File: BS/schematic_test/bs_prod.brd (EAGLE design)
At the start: 92 x 50 mm, 20 parts, among them U1 ATMEGA328P_PDIP, U2 RFM69HW, Y1 16MHz

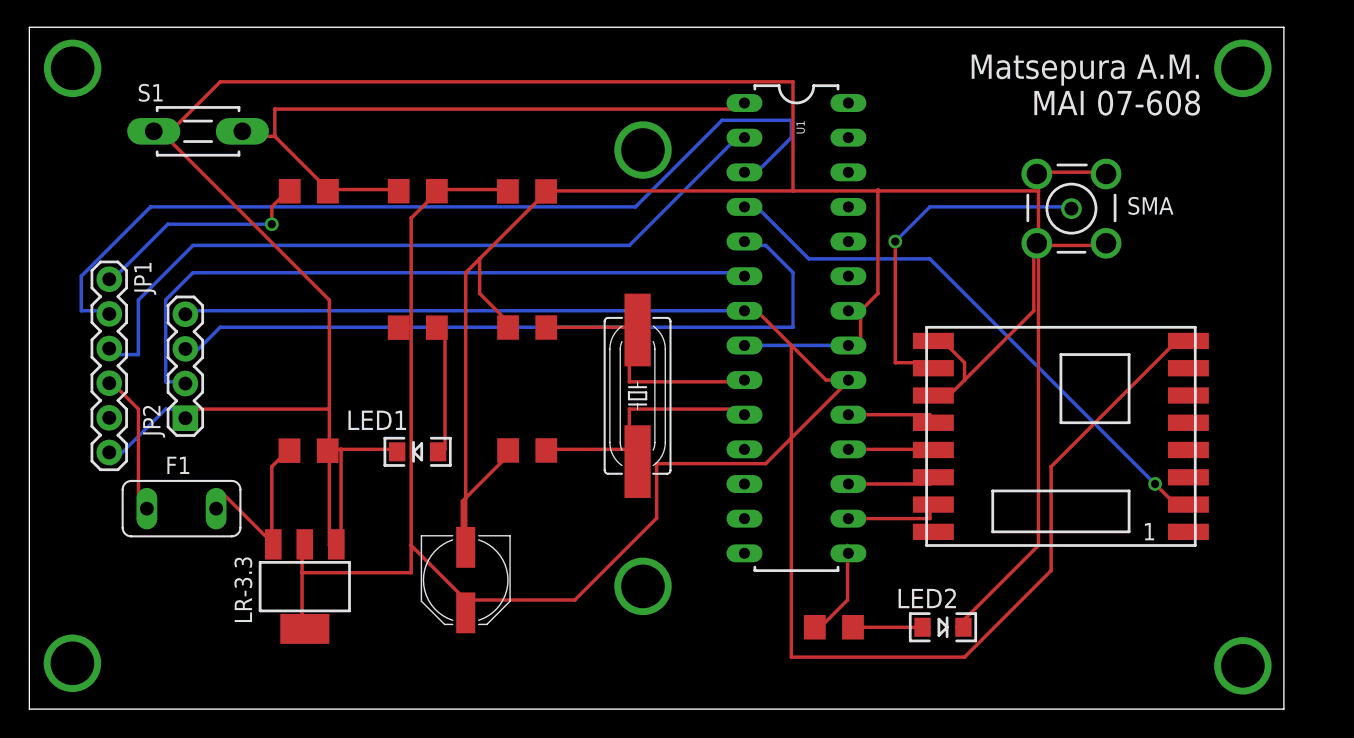
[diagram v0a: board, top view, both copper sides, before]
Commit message: BS schematic prod test add
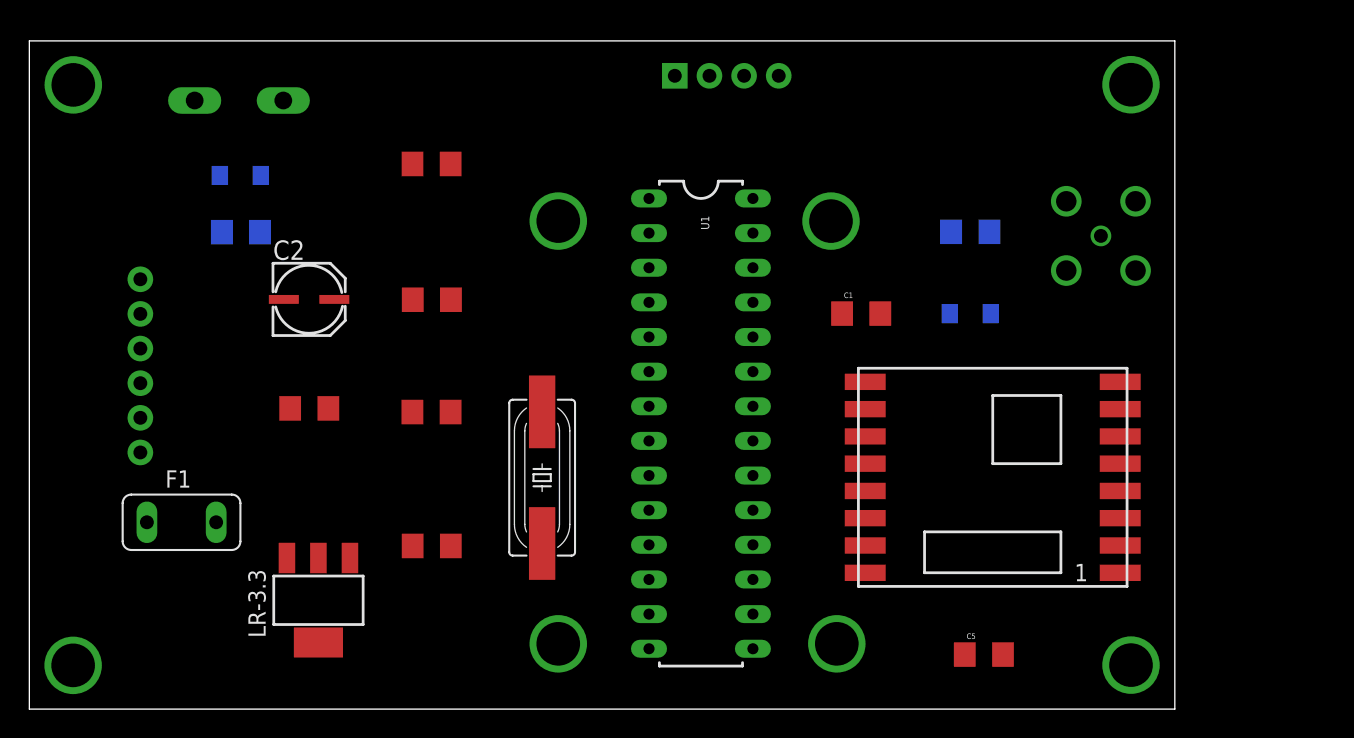
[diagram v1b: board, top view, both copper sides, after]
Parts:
- added C2: (no value), SparkFun-Capacitors:PANASONIC_C
- C1: value 10uF -> 0.1uF; device SparkFun-Capacitors:PANASONIC_D -> SparkFun-Capacitors:1206
- F1: value 500мА -> 500mA
- moved C5 47.7 mm to (70.0, 4.00)
- moved JP2 43.8 mm to (47.3, 46.4), flipped to the bottom, turned to 180 degrees
- moved C1 35.0 mm to (61.0, 29.0), turned to 0 degrees
- moved R3 30.7 mm to (69.0, 35.0), flipped to the bottom, turned to 180 degrees
- moved LED1 24.1 mm to (15.5, 39.1), flipped to the bottom, turned to 0 degrees
- moved LED2 23.1 mm to (69.0, 29.0), flipped to the bottom, turned to 180 degrees
- moved R2 14.7 mm to (15.5, 35.0), flipped to the bottom
- moved C4 9.90 mm to (29.5, 12.0)
- moved U1 9.90 mm to (49.3, 20.9)
- moved C3 9.36 mm to (29.5, 21.8)
- moved C6 9.22 mm to (29.5, 40.0)
- moved Y1 9.22 mm to (37.6, 17.0)
- moved R1 8.03 mm to (29.5, 30.0), turned to 0 degrees
- moved U2 5.83 mm to (70.6, 17.0)
- moved S1 3.76 mm to (15.4, 44.6), flipped to the bottom, turned to 0 degrees
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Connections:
- new net N$16: C1.1, U1.21
- net 3.3V: now also C2.+; no longer C1.+
- net GND: now also C1.2, C2.-; no longer C1.-, U1.21
- net GPS_RX: now also U1.5; no longer U1.6
- net GPS_TX: now also U1.6; no longer U1.5
- net N$12: now also U1.23; no longer U1.15
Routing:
- net GND: track 294.6 -> 0.00 mm
- net 3.3V: track 212.0 -> 0.00 mm
- net D1_TX: track 67.2 -> 0.00 mm
- net D0_RX: track 55.9 -> 0.00 mm
- net GPS_TX: track 54.9 -> 0.00 mm
- net GPS_RX: track 51.9 -> 0.00 mm
- net RST: track 50.8 -> 0.00 mm
- net D2: track 41.5 -> 0.00 mm, vias 1 -> 0
- net N$8: track 25.9 -> 0.00 mm, vias 1 -> 0
- net N$7: track 20.0 -> 0.00 mm
- net N$6: track 19.1 -> 0.00 mm
- net N$11: track 16.7 -> 0.00 mm, vias 1 -> 0
- net 5V: track 14.7 -> 0.00 mm
- net N$9: track 11.9 -> 0.00 mm
- net N$5: track 10.0 -> 0.00 mm
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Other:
- board size 92 x 50 mm -> 84 x 49 mm
- board text removed: "Matsepura A.M. MAI 07-608"

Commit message: BS schematic prod
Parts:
- removed LED1: (no value), SparkFun-LED:LED-1206
- removed S1: DTS-3, switch-tact:DTS-3
- added C8, C9: 0.1uF, SparkFun-Capacitors:1206
- added JP3: (no value), SparkFun-Connectors:1X06
- added JP4: (no value), SparkFun-Connectors:1X05
- added PWR: (no value), SparkFun-LED:LED-1206
- added RESET: DTSM-3, switch-tact:DTSM-3
- added U$1: UBLOX, myGps:UBLOX
- C2: value (none) -> 10uF
- moved R2 29.8 mm to (8.51, 5.97)
- moved C5 28.1 mm to (81.0, 29.8), turned to 180 degrees
- moved C2 13.8 mm to (32.9, 24.3)
- moved JP1 13.7 mm to (3.86, 18.5), turned to 90 degrees
- moved C7 13.4 mm to (32.5, 16.0), turned to 0 degrees
- moved F1 12.7 mm to (20.2, 4.70)
- moved LED2 12.2 mm to (81.0, 31.0)
- moved R3 12.0 mm to (81.0, 36.0)
- moved LR-3.3 11.0 mm to (32.2, 6.98)
- moved C1 11.0 mm to (72.0, 30.0), turned to 270 degrees
- moved U1 11.0 mm to (60.3, 21.9)
- moved C3 11.0 mm to (40.5, 21.8)
- moved C6 11.0 mm to (40.5, 40.0)
- moved C4 11.0 mm to (40.5, 12.0)
- moved SMA 11.0 mm to (89.6, 34.7)
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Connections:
- new net A0: JP3.4, U1.28
- new net A1: JP3.3, U1.27
- new net A2: JP3.2, U1.26
- new net A3: JP3.1, U1.25
- new net D5: JP4.1, U1.11
- new net D6: JP4.2, U1.12
- new net D7: JP4.3, U1.13
- net 3.3V: now also C8.1, C9.1, JP3.5, JP4.4
- net GND: now also C8.2, C9.2, JP3.6, JP4.5, PWR.C, RESET.2; no longer LED1.C, S1.2
- net N$5: now also PWR.A; no longer LED1.A
- net RST: now also RESET.1; no longer S1.1
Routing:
- net GND: track 0.00 -> 335.6 mm, vias 0 -> 2
- net 3.3V: track 0.00 -> 233.8 mm, vias 0 -> 5
- net N$11: track 0.00 -> 59.2 mm, vias 0 -> 1
- net D0_RX: track 0.00 -> 57.7 mm
- net D1_TX: track 0.00 -> 57.7 mm
- net D2: track 0.00 -> 46.0 mm, vias 0 -> 1
- net RST: track 0.00 -> 44.1 mm, vias 0 -> 1
- net D5: track 0.00 -> 35.1 mm
- net D6: track 0.00 -> 33.1 mm
- net A3: track 0.00 -> 31.5 mm
- net D7: track 0.00 -> 29.2 mm
- net A2: track 0.00 -> 27.7 mm
- net N$9: track 0.00 -> 27.1 mm
- net N$8: track 0.00 -> 26.4 mm, vias 0 -> 1
- net A1: track 0.00 -> 23.2 mm
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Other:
- board size 84 x 49 mm -> 95 x 49 mm
- board text added: "+5V"
- board text added: "3V3"
- board text added: "A2"
- board text added: "A3"
- board text added: "CTS"
- board text added: "D5"
- board text added: "D6"
- board text added: "D7"
- board text added: "DTR"
- board text added: "GND"
- board text added: "Matsepura A.M. MAI 07-608"
- board text added: "RX"
- board text added: "SCL"
- board text added: "SDA"
- board text added: "TX"
- board text added: "TX\"

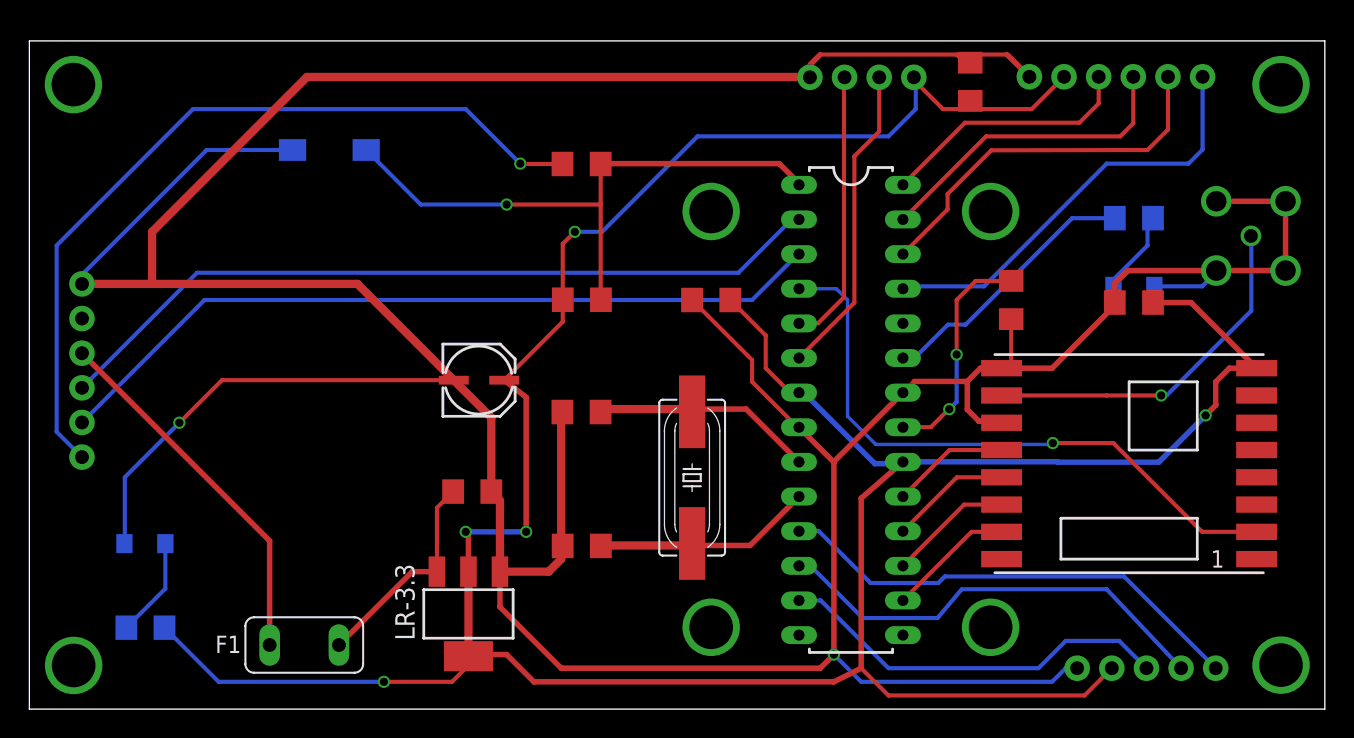
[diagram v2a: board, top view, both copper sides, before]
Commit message: add polygon to BS schematic
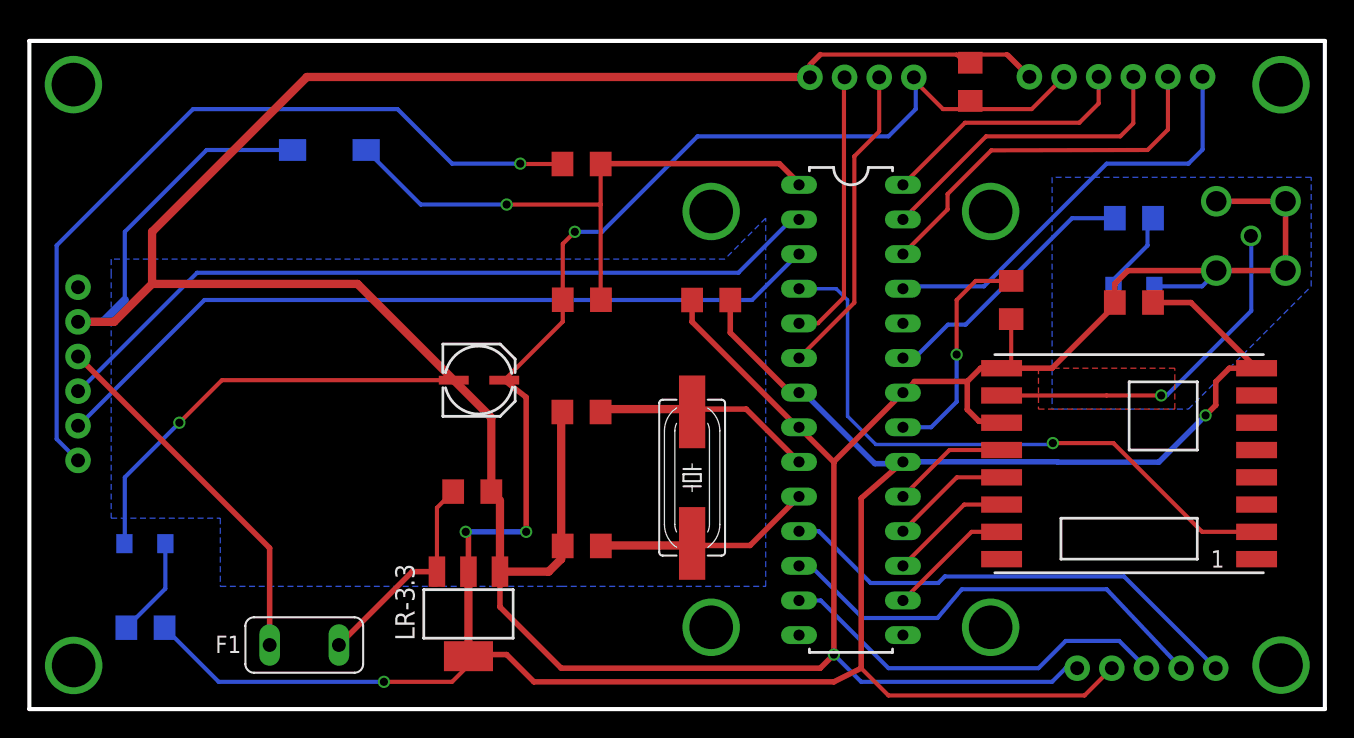
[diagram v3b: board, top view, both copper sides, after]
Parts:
- removed JP1: (no value), SparkFun-Connectors:1X06
- added JP5: (no value), SparkFun-Connectors:1X06
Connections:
- net D0_RX: now also JP5.3; no longer JP1.3
- net D1_TX: now also JP5.2; no longer JP1.2
- net GND: now also JP5.5; no longer JP1.6
- net N$11: now also JP5.1; no longer JP1.1
- net N$9: now also JP5.4; no longer JP1.4
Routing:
- net GND: track 335.6 -> 341.0 mm
- net N$16: vias 2 -> 1
- added copper zone on layer 16, net GND
- added copper zone on layer 1, net N$18
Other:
- board text removed: "CTS"

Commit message: final BS schematic
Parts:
- C9: value 0.1uF -> 0.47uF
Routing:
- net 3.3V: track 233.8 -> 234.6 mm
- net RST: track 44.1 -> 43.4 mm
- net GND: track 341.0 -> 341.6 mm
- added copper zone on layer 1, net GND
- removed copper zone on layer 1, net N$18
